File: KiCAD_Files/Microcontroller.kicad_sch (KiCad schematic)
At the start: 3 parts, among them U901 OwnTech_SPIN

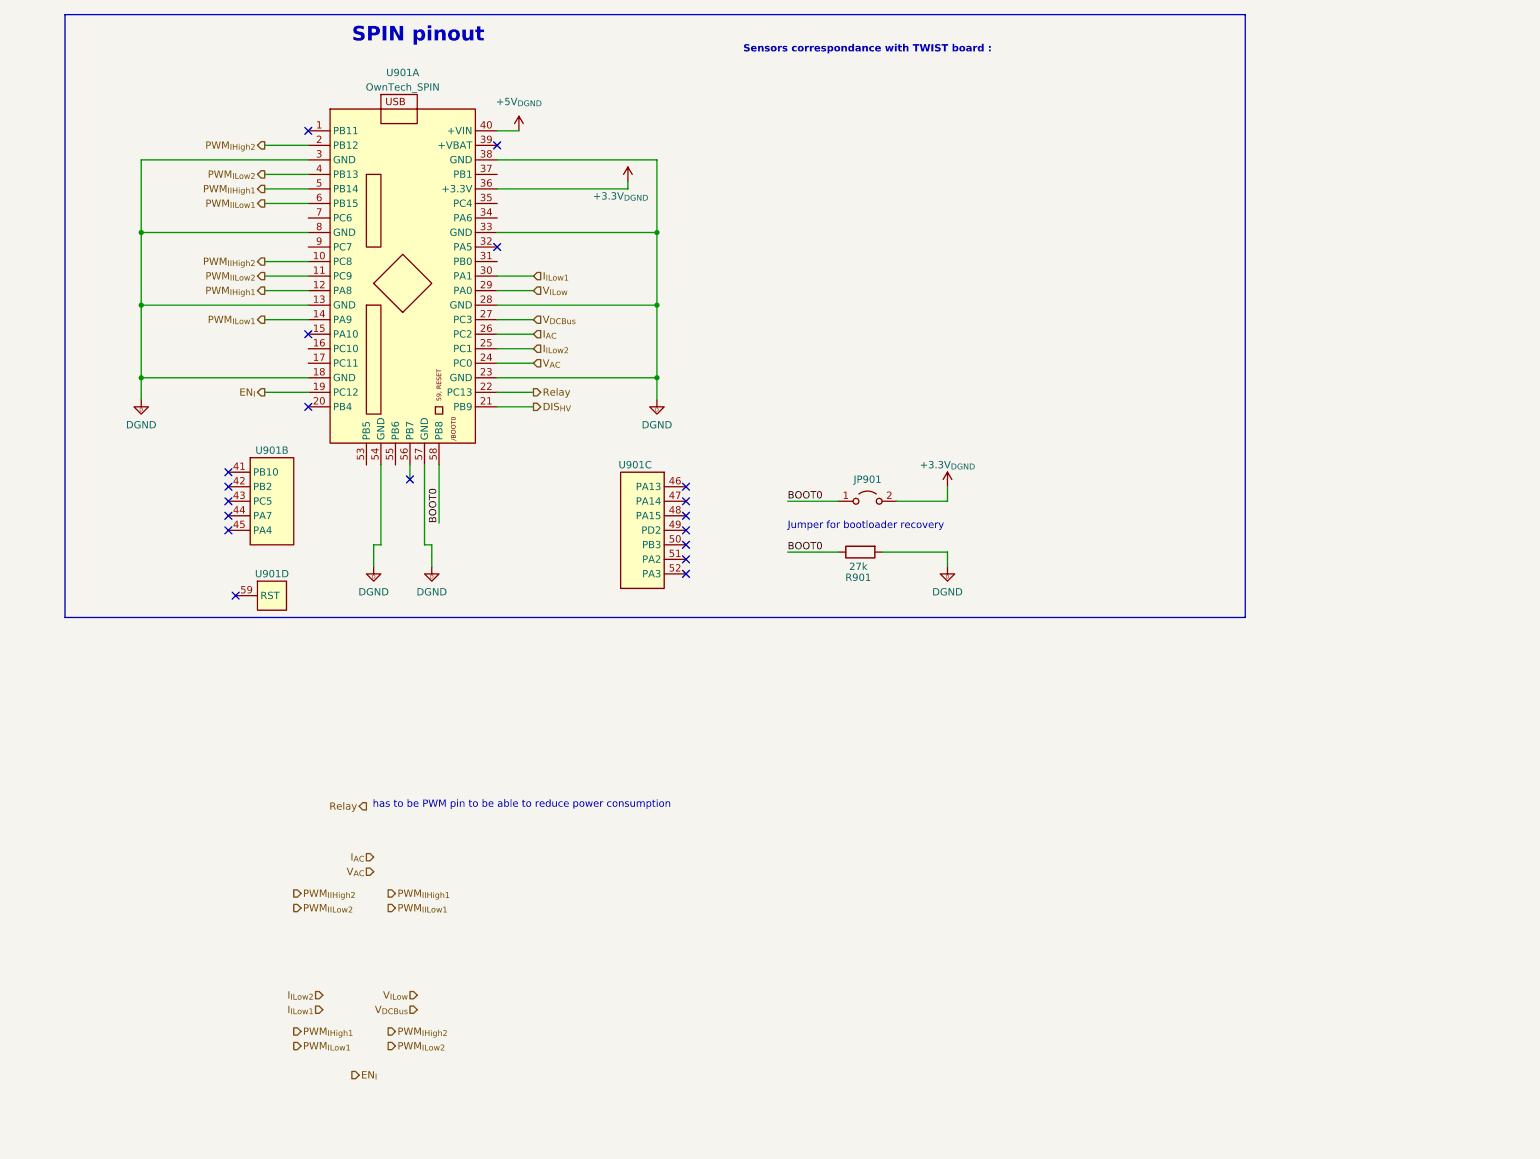
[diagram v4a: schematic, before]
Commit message: Added passive references. Added ESD protection for MCU pins.
Signed-off-by: Jean Alinei <jean.alinei@owntech.org>
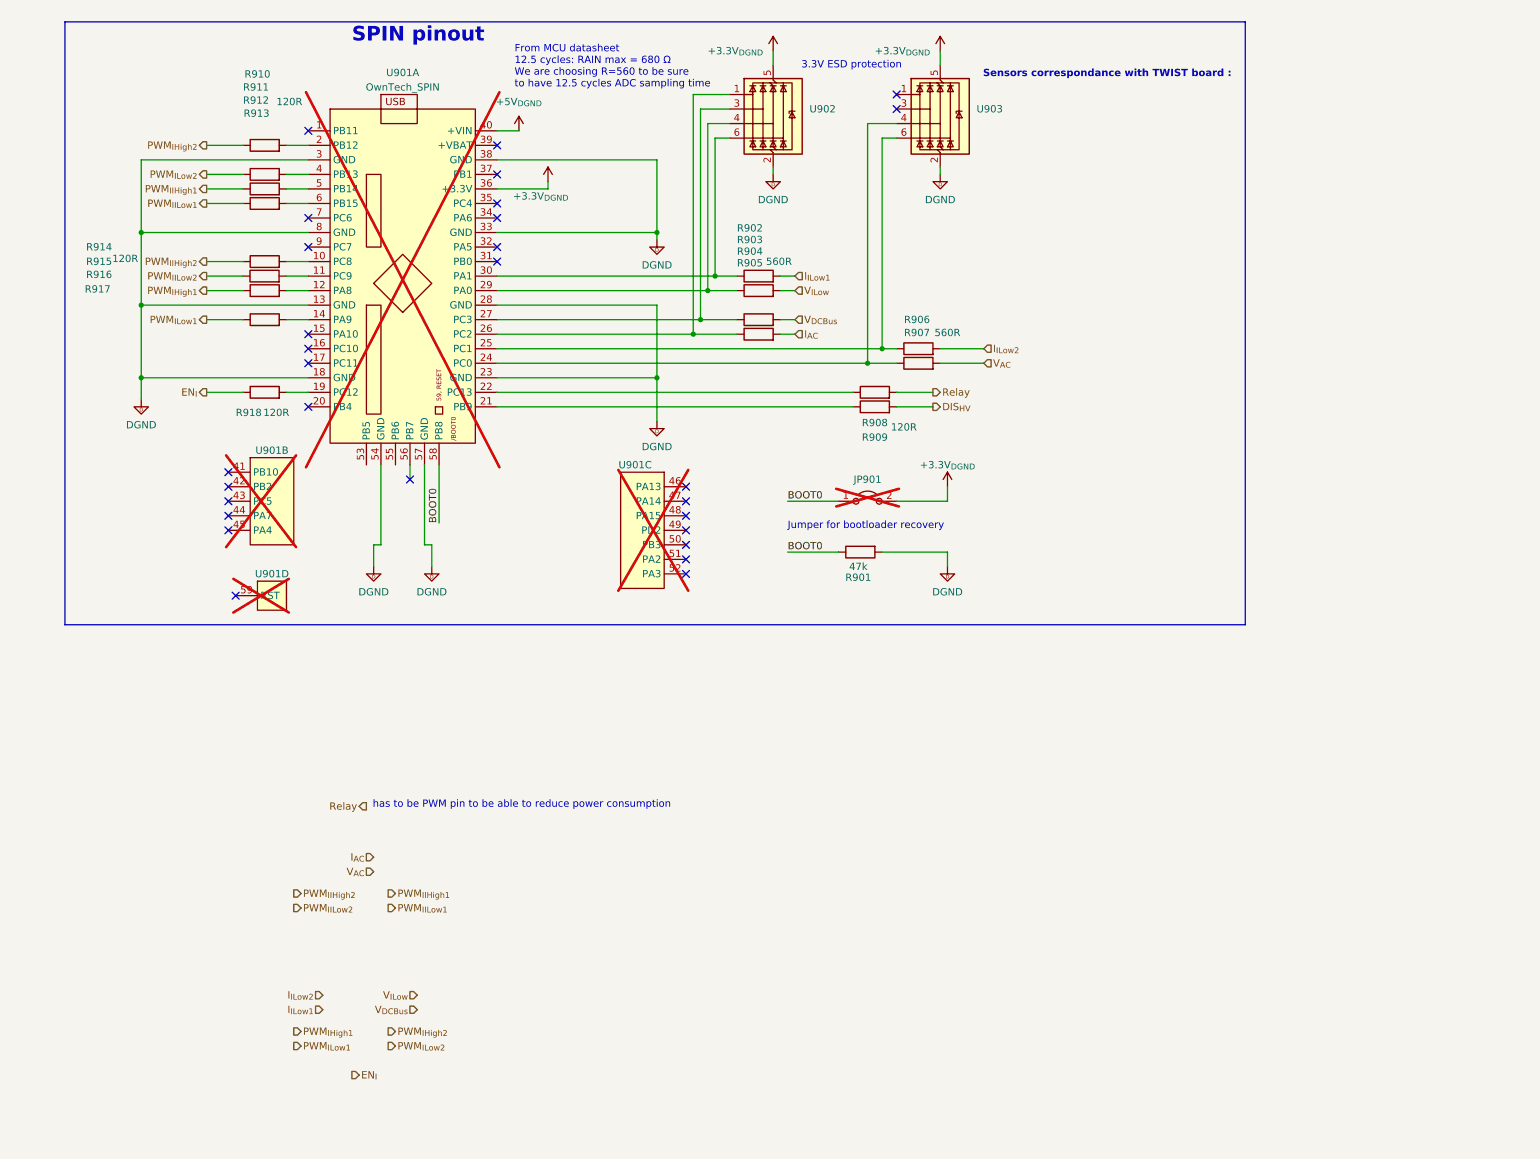
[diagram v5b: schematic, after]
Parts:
- added R902, R903, R904, R905, R906, R907: 560R, Footprints:R_0805_2012Metric, symbol Device:R
- added R908, R909, R910, R911, R912, R913, R914, R915, R916, R917, R918: 120R, Footprints:R_0805_2012Metric, symbol Device:R
- added U902, U903: WE-TVS-824015043, Package_TO_SOT_SMD:SOT-363_SC-70-6, symbol Power_Protection:WE-TVS-824015043
- JP901: now not fitted
- R901: value 27k -> 47k; LCSC (none) -> C17713; Metal content NiCr -> (none); Package 0805 -> (none); Subfunction Analog bus -> (none); Technology Thick film -> (none); manf# CR0805-FX-4701ELF -> (none)
- U901: manf# SPIN -> (none); now not fitted
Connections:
- net +3.3V_{DGND}: now also U902.5 (VBUS), U903.5 (VBUS)
- net DGND: now also U902.2 (GND), U903.2 (GND)
- net DIS_{HV}: now also R909.2; no longer U901.21 (PB9)
- net EN_{I}: now also R918.1; no longer U901.19 (PC12)
- net I_{AC}: now also R905.2; no longer U901.26 (PC2)
- net I_{ILow1}: now also R902.2; no longer U901.30 (PA1)
- net I_{ILow2}: now also R906.2; no longer U901.25 (PC1)
- net PWM_{IHigh1}: now also R916.1; no longer U901.12 (PA8)
- net PWM_{IHigh2}: now also R910.1; no longer U901.2 (PB12)
- net PWM_{IIHigh1}: now also R912.1; no longer U901.5 (PB14)
- net PWM_{IIHigh2}: now also R914.1; no longer U901.10 (PC8)
- net PWM_{IILow1}: now also R913.1; no longer U901.6 (PB15)
- net PWM_{IILow2}: now also R915.1; no longer U901.11 (PC9)
- net PWM_{ILow1}: now also R917.1; no longer U901.14 (PA9)
- net PWM_{ILow2}: now also R911.1; no longer U901.4 (PB13)
- net Relay: now also R908.2; no longer U901.22 (PC13)
- net V_{AC}: now also R907.2; no longer U901.24 (PC0)
- net V_{DCBus}: now also R904.2; no longer U901.27 (PC3)
- net V_{ILow}: now also R903.2; no longer U901.29 (PA0)
- new net: R905.1, U901.26 (PC2), U902.1 (I/O1)
- new net: R904.1, U901.27 (PC3), U902.3 (I/O2)
- new net: R903.1, U901.29 (PA0), U902.4 (I/O3)
- new net: R902.1, U901.30 (PA1), U902.6 (I/O4)
- new net: R911.2, U901.4 (PB13)
- new net: R910.2, U901.2 (PB12)
- new net: R916.2, U901.12 (PA8)
- new net: R907.1, U901.24 (PC0), U903.4 (I/O3)
- new net: R906.1, U901.25 (PC1), U903.6 (I/O4)
- new net: R909.1, U901.21 (PB9)
- new net: R912.2, U901.5 (PB14)
- new net: R917.2, U901.14 (PA9)
- new net: R918.2, U901.19 (PC12)
- new net: R913.2, U901.6 (PB15)
- new net: R914.2, U901.10 (PC8)
- new net: R915.2, U901.11 (PC9)
- new net: R908.1, U901.22 (PC13)
- no-connect marks 19 -> 29
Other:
- note added: "3.3V ESD protection"
- note added: "From MCU datasheet 12.5 cycles: RAIN max = 680 Ω We are choosing R=560 to be sure to have 12.5 cycles ADC sampling time"

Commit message: Added TL431 for AC measurement 5V regulation. Added more film capacitance. Increased size of 100V ceramic caps to 1210.
Signed-off-by: Jean Alinei <jean.alinei@owntech.org>
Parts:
- U901: symbol Symbols:OwnTech_SPIN -> Symbols:OwnTech_SPIN2
- U902, U903: symbol Power_Protection:WE-TVS-824015043 -> Symbols:TVS-4-ways
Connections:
- no-connect marks 29 -> 31

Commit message: Tidied up the schematic. Added the pdf version for V0.9.
Signed-off-by: Jean Alinei <jean.alinei@owntech.org>
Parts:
- U901: now fitted
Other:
- title: Micro-inverter - 400W -> Power stage controller
- moved on the sheet: JP901, R901, R902, R903, R904, R905, R906, R907, R908, R909, R910, R911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
